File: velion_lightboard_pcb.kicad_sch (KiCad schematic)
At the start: 49 parts, among them J1 Conn_01x04, J10 Conn_01x03, J11 Conn_01x03, J2 Conn_01x04, J3 Conn_01x03, J4 Conn_01x03, J5 Conn_01x03, J6 Conn_01x03, J7 Conn_01x03, J8 Conn_01x03, J9 Conn_01x03, Q1 NMOS, Q2 NMOS, Q3 NMOS, Q4 NMOS, Q5 NMOS, Q6 NMOS, Q7 NMOS, Q8 NMOS, U1 TJA1051T-3, U6 ESP32-DEVKITC-32D, U7 MCP23017_SO, U8 MCP23017_SO

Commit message: switched MCU, implemented led driver, TODO : rangerfinder
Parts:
- removed R3, R4, R5: 100R, Resistor_SMD:R_1206_3216Metric_Pad1.30x1.75mm_HandSolder, symbol Device:R
- removed U6: ESP32-DEVKITC-32D, velion_mainboard:MODULE_ESP32-DEVKITC-32D, symbol ESP32-DEVKITC-32D:ESP32-DEVKITC-32D
- removed U7: MCP23017_SO, Package_SO:SOIC-28W_7.5x17.9mm_P1.27mm, symbol Interface_Expansion:MCP23017_SO
- added C3, C4: 100nF, symbol Device:C
- added J12: Conn_01x04, symbol Connector_Generic:Conn_01x04
- added LS1, LS2, LS3, LS4: Speaker_Ultrasound, symbol Device:Speaker_Ultrasound
- added U2, U3: ADS1115IDGS, Package_SO:TSSOP-10_3x3mm_P0.5mm, symbol Analog_ADC:ADS1115IDGS
- added U4: ESP32-C3_SUPERMINI_TH, ESP32-C3_SUPERMINI_TH:MODULE_ESP32-C3_SUPERMINI_TH, symbol ESP32-C3_SUPERMINI_TH:ESP32-C3_SUPERMINI_TH
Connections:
- net +3.3V: now also C3.1, C4.1, J12.3 (Pin_3), U2.8 (VDD), U3.1 (ADDR), U3.8 (VDD), U4.3.3 (3V3)
- net CAN_RX: now also U4.3 (GPIO3)
- net CAN_S: now also U4.7 (GPIO7)
- net CAN_TX: now also U4.2 (GPIO2)
- net GND: now also C3.2, C4.2, J12.4 (Pin_4), U2.1 (ADDR), U2.3 (GND), U3.3 (GND), U4.G (GND)
- net RGBLED_DIN: now also U4.8 (GPIO8)
- net SCL: now also J12.2 (Pin_2), U2.10 (SCL), U3.10 (SCL), U4.1 (GPIO1)
- net SDA: now also J12.1 (Pin_1), U2.9 (SDA), U3.9 (SDA), U4.0 (GPIO0)
- net MOSFET_GATE_0: now reaches U8.1 (GPB0)
- net MOSFET_GATE_0: now also Q6.1 (G)
- net MOSFET_GATE_1: now reaches U8.2 (GPB1)
- net MOSFET_GATE_1: now also Q5.1 (G)
- net MOSFET_GATE_2: now reaches U8.3 (GPB2)
- net MOSFET_GATE_2: now also Q4.1 (G)
- net MOSFET_GATE_3: now reaches U8.4 (GPB3)
- net MOSFET_GATE_3: now also Q3.1 (G)
- net MOSFET_GATE_4: now reaches U8.5 (GPB4)
- net MOSFET_GATE_4: now also Q2.1 (G)
- net MOSFET_GATE_5: now reaches U8.6 (GPB5)
- net MOSFET_GATE_5: now also Q1.1 (G)
- net MOSFET_GATE_6: now reaches U8.7 (GPB6)
- net MOSFET_GATE_6: now also Q8.1 (G)
- net MOSFET_GATE_7: now reaches U8.8 (GPB7)
- net MOSFET_GATE_7: now also Q7.1 (G)
- removed net LATCH_TRUNK_MOSFET_GATE: Q1.1 (G), Q2.1 (G), Q3.1 (G), Q4.1 (G), Q5.1 (G), Q6.1 (G), Q7.1 (G), Q8.1 (G)
- removed net SENSE: J10.3 (Pin_3), J11.3 (Pin_3), J4.3 (Pin_3), J5.3 (Pin_3), J6.3 (Pin_3), J7.3 (Pin_3), J8.3 (Pin_3), J9.3 (Pin_3), Q1.2 (S), Q2.2 (S), Q3.2 (S), Q4.2 (S), Q5.2 (S), Q6.2 (S), Q7.2 (S), Q8.2 (S), R14.1, R15.1, R16.1, R17.1, R19.1, R20.1, R21.1, R22.1
- new net SENSE_0: J10.3 (Pin_3), Q6.2 (S), R14.1, U2.4 (AIN0)
- new net SENSE_1: J9.3 (Pin_3), Q5.2 (S), R15.1, U2.5 (AIN1)
- new net SENSE_2: J8.3 (Pin_3), Q4.2 (S), R16.1, U2.6 (AIN2)
- new net SENSE_3: J7.3 (Pin_3), Q3.2 (S), R17.1, U2.7 (AIN3)
- new net SENSE_4: J6.3 (Pin_3), Q2.2 (S), R19.1, U3.4 (AIN0)
- new net SENSE_5: J5.3 (Pin_3), Q1.2 (S), R20.1, U3.5 (AIN1)
- new net SENSE_6: J4.3 (Pin_3), Q8.2 (S), R21.1, U3.6 (AIN2)
- new net SENSE_7: J11.3 (Pin_3), Q7.2 (S), R22.1, U3.7 (AIN3)
- no-connect marks 13 -> 5
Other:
- note added: "I2C addr : 1001000-> 0x48"
- note added: "I2C addr : 1001001-> 0x49"
- note added: "SDA SCL GND 3V3"
- note removed: "0100001 = 0x21"
- note removed: "leave serial port for debug"
- note removed: "resistor to limit risk of issue due to current leakage and the mosfet grid capacitor that could influence the strapping pin at boot."
- moved on the sheet: R6, R7

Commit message: Implemented piezo sonar driver
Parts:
- removed LS4: Speaker_Ultrasound, symbol Device:Speaker_Ultrasound
- added C10, C11, C12, C13, C14, C15, C16, C5, C6, C7, C8, C9: 100nF, symbol Device:C
- added D1, D2, D3, D6, D7, D8: D, symbol Device:D
- added J13, J14, J15: Conn_01x04, symbol Connector_Generic:Conn_01x04
- added Q10, Q11, Q12, Q13, Q14, Q15, Q16, Q17, Q18, Q19, Q20, Q9: BSS123-7-F, symbol Device:Q_NMOS
- added R23, R24, R25, R26, R27, R28, R29, R3, R30, R31, R4, R5: 470R, symbol Device:R
- added U10, U11, U5, U6, U7, U9: ~, symbol velion_mainboard:LM2104
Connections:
- net +12V: now also C12.1, C13.1, C16.1, C6.1, C7.1, C9.1, D1.2 (A), D2.2 (A), D3.2 (A), D6.2 (A), D7.2 (A), D8.2 (A), U10.1 (GVDD), U11.1 (GVDD), U5.1 (GVDD), U6.1 (GVDD), U7.1 (GVDD), U9.1 (GVDD)
- net +5V: now also U4.5V, J13.1 (Pin_1), J14.1 (Pin_1), J15.1 (Pin_1)
- net GND: now also C12.2, C13.2, C16.2, C6.2, C7.2, C9.2, J13.4 (Pin_4), J14.4 (Pin_4), J15.4 (Pin_4), Q10.S, Q12.S, Q14.S, Q16.S, Q18.S, Q20.S, U10.4 (GND), U11.4 (GND), U5.4 (GND), U6.4 (GND), U7.4 (GND), U9.4 (GND)
- net VBUS: now also Q11.D, Q13.D, Q15.D, Q17.D, Q19.D, Q9.D
- net ECHO_B: now reaches U4.10 (GPIO10)
- net ECHO_B: now also J14.3 (Pin_3)
- net ECHO_A: now reaches U4.20 (GPIO20)
- net ECHO_A: now also J15.3 (Pin_3)
- net TRIG_A: now reaches U4.4 (GPIO4)
- net TRIG_A: now also J15.2 (Pin_2)
- net TRIG_B: now reaches U4.5 (GPIO5)
- net TRIG_B: now also J14.2 (Pin_2)
- net TRIG_C: now reaches U4.6 (GPIO6)
- net TRIG_C: now also J13.2 (Pin_2)
- net ECHO_C: now reaches U4.9 (GPIO9)
- net ECHO_C: now also J13.3 (Pin_3)
- net EN_PIEZO_A: now reaches U8.21 (GPA0)
- net EN_PIEZO_A: now also U5.3 (~{SD}), U6.3 (~{SD})
- net EN_PIEZO_B: now reaches U8.22 (GPA1)
- net EN_PIEZO_B: now also U7.3 (~{SD}), U9.3 (~{SD})
- net EN_PIEZO_C: now reaches U8.23 (GPA2)
- net EN_PIEZO_C: now also U10.3 (~{SD}), U11.3 (~{SD})
- net EN_PIEZO_D: now reaches U8.24 (GPA3)
- net at LS1.1: now also Q13.S, Q14.D
- net at LS1.2: now also Q15.S, Q16.D
- net at LS3.1: now also Q10.D, Q9.S
- net at LS3.2: now also Q11.S, Q12.D
- net at LS2.1: now also Q17.S, Q18.D
- net at LS2.2: now also Q19.S, Q20.D
- new net: Q9.G, R3.2
- new net: R30.1, U11.5 (GL)
- new net: C15.2, U11.6 (SH)
- new net: R31.1, U11.7 (GH)
- new net: C15.1, D8.1 (K), U11.8 (BST)
- new net: Q16.G, R26.2
- new net: Q13.G, R24.2
- new net: Q19.G, R31.2
- new net: R23.1, U6.5 (GL)
- new net: Q12.G, R23.2
- new net: R25.1, U7.5 (GL)
- new net: C10.2, U7.6 (SH)
- new net: R24.1, U7.7 (GH)
- new net: C10.1, D3.1 (K), U7.8 (BST)
- new net: R29.1, U10.5 (GL)
- new net: C14.2, U10.6 (SH)
- new net: R28.1, U10.7 (GH)
- new net: C14.1, D7.1 (K), U10.8 (BST)
- new net: R5.1, U6.7 (GH)
- new net: Q11.G, R5.2
- new net: R3.1, U5.7 (GH)
- new net: C5.1, D1.1 (K), U5.8 (BST)
- new net: C5.2, U5.6 (SH)
- new net: R26.1, U9.5 (GL)
- new net: C11.2, U9.6 (SH)
- new net: R27.1, U9.7 (GH)
- new net: C11.1, D6.1 (K), U9.8 (BST)
- new net: Q10.G, R4.2
- new net: Q20.G, R30.2
- new net: Q18.G, R29.2
- new net: Q17.G, R28.2
- new net: C8.1, D2.1 (K), U6.8 (BST)
- new net: Q15.G, R27.2
- new net: C8.2, U6.6 (SH)
- new net: R4.1, U5.5 (GL)
- new net: Q14.G, R25.2
- new net PIEZO_PWM_HALF_X: U10.2 (IN), U5.2 (IN), U7.2 (IN)
- new net PIEZO_PWM_HALF_Y: U11.2 (IN), U6.2 (IN), U9.2 (IN)
- no-connect marks 5 -> 4
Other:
- note added: "3v3 come from ESP32-C internal regulator"
- note added: "5V TRIG ECHO GND"
- note added: "ADC for current sensing"
- note added: "GPIO"
- note added: "backup: if the driver dont work, we can use off the shelf module."
- note added: "classic bootstap capacitor setup"
- note added: "lightning"
- note added: "theses resistor are to limit EMI"
- note removed: "add ADC here with 8 channel"
- moved on the sheet: C3, C4, J12, U2, U3, U8

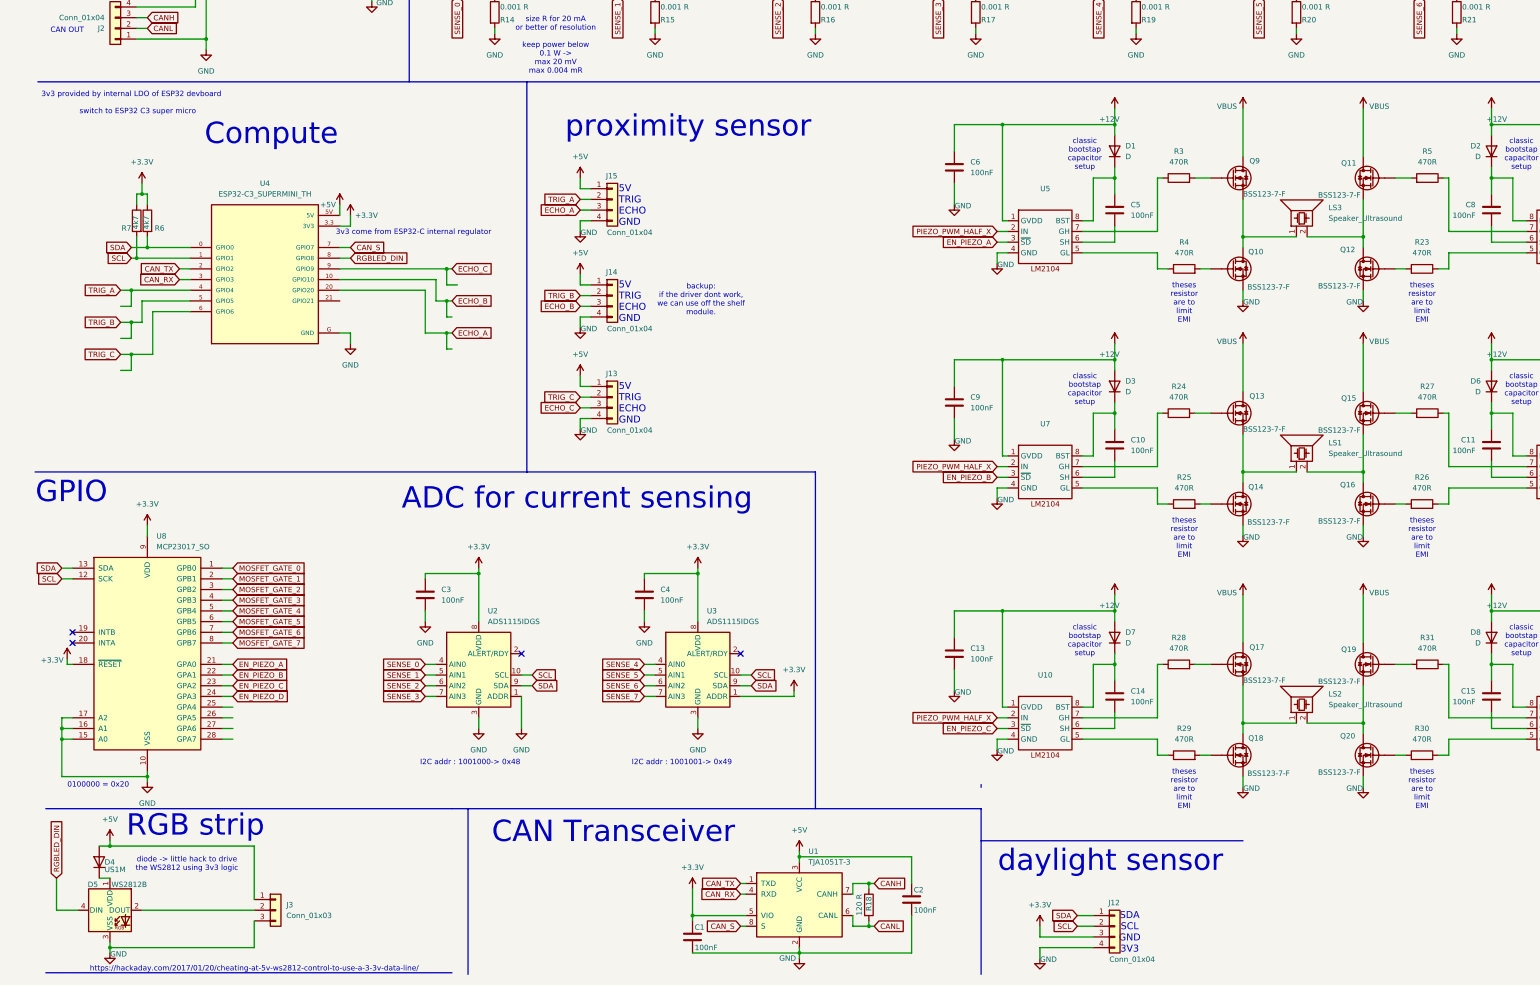
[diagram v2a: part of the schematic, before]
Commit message: implemented Analog stage for piezzo sonar
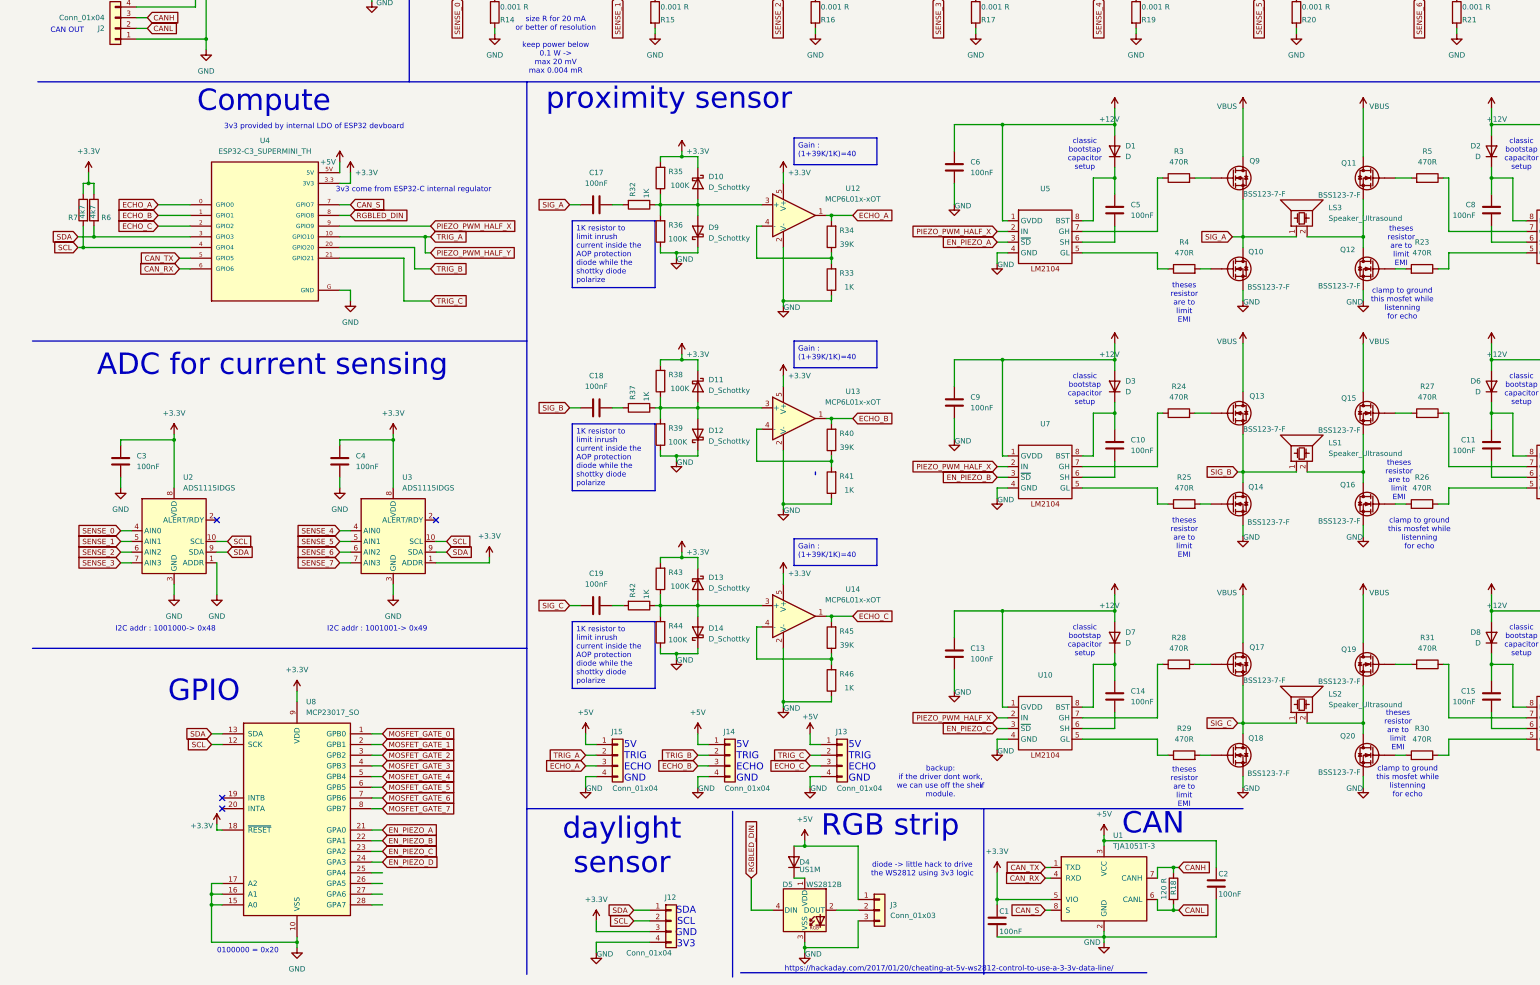
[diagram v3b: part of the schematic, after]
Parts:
- added C17, C18, C19: 100nF, symbol Device:C
- added D10, D11, D12, D13, D14, D9: D_Schottky, symbol Device:D_Schottky
- added R32, R33, R37, R41, R42, R46: 1K, symbol Device:R
- added R34, R40, R45: 39K, symbol Device:R
- added R35, R36, R38, R39, R43, R44: 100K, symbol Device:R
- added U12, U13, U14: MCP6L01x-xOT, Package_TO_SOT_SMD:SOT-23-5, symbol Amplifier_Operational:MCP6L01x-xOT
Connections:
- net +3.3V: now also D10.1 (K), D11.1 (K), D13.1 (K), R35.2, R38.2, R43.2, U12.5 (V+), U13.5 (V+), U14.5 (V+)
- net CAN_RX: now also U4.6 (GPIO6); no longer U4.3 (GPIO3)
- net CAN_TX: now also U4.5 (GPIO5); no longer U4.2 (GPIO2)
- net ECHO_A: now also U4.0 (GPIO0), R34.2, U12.1; no longer U4.20 (GPIO20)
- net ECHO_B: now also U4.1 (GPIO1), R40.2, U13.1; no longer U4.10 (GPIO10)
- net ECHO_C: now also U4.2 (GPIO2), R45.2, U14.1; no longer U4.9 (GPIO9)
- net GND: now also D12.1 (K), D14.1 (K), D9.1 (K), R33.1, R36.1, R39.1, R41.1, R44.1, R46.1, U12.2 (V-), U13.2 (V-), U14.2 (V-)
- net PIEZO_PWM_HALF_X: now also U4.9 (GPIO9)
- net PIEZO_PWM_HALF_Y: now also J15.2 (Pin_2), U4.10 (GPIO10)
- net SCL: now also U4.4 (GPIO4); no longer U4.1 (GPIO1)
- net SDA: now also U4.3 (GPIO3); no longer U4.0 (GPIO0)
- net TRIG_B: now also U4.20 (GPIO20); no longer U4.5 (GPIO5)
- net TRIG_C: now also U4.21 (GPIO21); no longer U4.6 (GPIO6)
- net SIG_A: now reaches LS3.1, Q10.D, Q9.S
- net SIG_A: now also C17.2
- net SIG_B: now reaches LS1.1, Q13.S, Q14.D
- net SIG_B: now also C18.2
- net SIG_C: now reaches LS2.1, Q17.S, Q18.D
- net SIG_C: now also C19.2
- removed net TRIG_A: J15.2 (Pin_2), U4.4 (GPIO4)
- new net: D13.2 (A), D14.2 (A), R42.1, R43.1, R44.2, U14.3 (+)
- new net: D11.2 (A), D12.2 (A), R37.1, R38.1, R39.2, U13.3 (+)
- new net: R45.1, R46.2, U14.4 (-)
- new net: R40.1, R41.2, U13.4 (-)
- new net: C18.1, R37.2
- new net: C17.1, R32.2
- new net: D10.2 (A), D9.2 (A), R32.1, R35.1, R36.2, U12.3 (+)
- new net: R33.2, R34.1, U12.4 (-)
- new net: C19.1, R42.2
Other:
- note added: "CAN"
- note added: "clamp to ground this mosfet while listenning for echo"
- note removed: "CAN Transceiver"
- note removed: "switch to ESP32 C3 super micro"
- moved on the sheet: C1, C2, C3, C4, D4, D5, J12, J13, J14, J15, J3, R18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

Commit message: layaing out the components
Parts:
- added J5, J6: Conn_01x04, velion_mainboard:15EDG-4P, symbol Connector_Generic:Conn_01x04
- C1: renamed from C9; footprint (none) -> Capacitor_SMD:C_1206_3216Metric_Pad1.33x1.80mm_HandSolder
- C10: renamed from C6; footprint (none) -> Capacitor_SMD:C_1206_3216Metric_Pad1.33x1.80mm_HandSolder
- C11: renamed from C5; footprint (none) -> Capacitor_SMD:C_1206_3216Metric_Pad1.33x1.80mm_HandSolder
- C12: renamed from C4; footprint (none) -> Capacitor_SMD:C_1206_3216Metric_Pad1.33x1.80mm_HandSolder
- C13: renamed from C14; footprint (none) -> Capacitor_SMD:C_1206_3216Metric_Pad1.33x1.80mm_HandSolder
- C14: renamed from C7; footprint (none) -> Capacitor_SMD:C_1206_3216Metric_Pad1.33x1.80mm_HandSolder
- C15: renamed from C17; footprint (none) -> Capacitor_SMD:C_1206_3216Metric_Pad1.33x1.80mm_HandSolder
- C16, C18, C19: footprint (none) -> Capacitor_SMD:C_1206_3216Metric_Pad1.33x1.80mm_HandSolder
- C17: renamed from C15; footprint (none) -> Capacitor_SMD:C_1206_3216Metric_Pad1.33x1.80mm_HandSolder
- C3: renamed from C10; footprint (none) -> Capacitor_SMD:C_1206_3216Metric_Pad1.33x1.80mm_HandSolder
- C4: renamed from C8; footprint (none) -> Capacitor_SMD:C_1206_3216Metric_Pad1.33x1.80mm_HandSolder
- C5: renamed from C3; footprint (none) -> Capacitor_SMD:C_1206_3216Metric_Pad1.33x1.80mm_HandSolder
- C7: renamed from C13; footprint (none) -> Capacitor_SMD:C_1206_3216Metric_Pad1.33x1.80mm_HandSolder
- C8: renamed from C12; footprint (none) -> Capacitor_SMD:C_1206_3216Metric_Pad1.33x1.80mm_HandSolder
- C9: renamed from C11; footprint (none) -> Capacitor_SMD:C_1206_3216Metric_Pad1.33x1.80mm_HandSolder
- D10: renamed from D3; footprint (none) -> Diode_SMD:D_SMA
- D11: renamed from D6; footprint (none) -> Diode_SMD:D_SMA
- D13: renamed from D8; footprint (none) -> Diode_SMD:D_SMA
- D14: renamed from D7; footprint (none) -> Diode_SMD:D_SMA
- D2: renamed from D9; value D_Schottky -> RB551V-30-HF; footprint (none) -> Diode_SMD:D_SOD-323_HandSoldering
- D3: renamed from D10; value D_Schottky -> RB551V-30-HF; footprint (none) -> Diode_SMD:D_SOD-323_HandSoldering
- D4: renamed from D11; value D_Schottky -> RB551V-30-HF; footprint (none) -> Diode_SMD:D_SOD-323_HandSoldering
- D5: renamed from D12; value D_Schottky -> RB551V-30-HF; footprint (none) -> Diode_SMD:D_SOD-323_HandSoldering
- D6: renamed from D13; value D_Schottky -> RB551V-30-HF; footprint (none) -> Diode_SMD:D_SOD-323_HandSoldering
- D7: renamed from D14; value D_Schottky -> RB551V-30-HF; footprint (none) -> Diode_SMD:D_SOD-323_HandSoldering
- D8: renamed from D2; footprint (none) -> Diode_SMD:D_SMA
- D9: renamed from D1; footprint (none) -> Diode_SMD:D_SMA
- J10: renamed from J14; footprint (none) -> Connector_PinHeader_2.54mm:PinHeader_1x04_P2.54mm_Vertical
- J11: renamed from J12; footprint (none) -> Connector_PinHeader_2.54mm:PinHeader_1x04_P2.54mm_Vertical
- J12: renamed from J6; footprint (none) -> velion_mainboard:15EDG-3P
- J13: renamed from J5; footprint (none) -> velion_mainboard:15EDG-3P
- J14: renamed from J3; footprint (none) -> velion_mainboard:15EDG-3P
- J15: renamed from J4; footprint (none) -> velion_mainboard:15EDG-3P
- J16: renamed from J11; footprint (none) -> velion_mainboard:15EDG-3P
- J17: renamed from J13; footprint (none) -> Connector_PinHeader_2.54mm:PinHeader_1x04_P2.54mm_Vertical
- J3: renamed from J10; footprint (none) -> velion_mainboard:15EDG-3P
- J4: renamed from J15; footprint (none) -> Connector_PinHeader_2.54mm:PinHeader_1x04_P2.54mm_Vertical
- J7: renamed from J9; footprint (none) -> velion_mainboard:15EDG-3P
- J8: footprint (none) -> velion_mainboard:15EDG-3P
- J9: renamed from J7; footprint (none) -> velion_mainboard:15EDG-3P
- LS1: renamed from LS3; footprint (none) -> velion_mainboard:15EDG-2P
- LS2: renamed from LS1; footprint (none) -> velion_mainboard:15EDG-2P
- LS3: renamed from LS2; footprint (none) -> velion_mainboard:15EDG-2P
- Q1: renamed from Q9; footprint (none) -> velion_mainboard:BSS123_TSOT-23_HandSoldering
- Q10: renamed from Q17; footprint (none) -> velion_mainboard:BSS123_TSOT-23_HandSoldering
- Q11: renamed from Q20; footprint (none) -> velion_mainboard:BSS123_TSOT-23_HandSoldering
- Q12: renamed from Q19; footprint (none) -> velion_mainboard:BSS123_TSOT-23_HandSoldering
- Q2: renamed from Q10; footprint (none) -> velion_mainboard:BSS123_TSOT-23_HandSoldering
- Q3: renamed from Q14; footprint (none) -> velion_mainboard:BSS123_TSOT-23_HandSoldering
- Q4: renamed from Q13; footprint (none) -> velion_mainboard:BSS123_TSOT-23_HandSoldering
- Q5: renamed from Q11; footprint (none) -> velion_mainboard:BSS123_TSOT-23_HandSoldering
- Q6: renamed from Q16; footprint (none) -> velion_mainboard:BSS123_TSOT-23_HandSoldering
- Q7: renamed from Q15; footprint (none) -> velion_mainboard:BSS123_TSOT-23_HandSoldering
- Q8: renamed from Q12; footprint (none) -> velion_mainboard:BSS123_TSOT-23_HandSoldering
- Q9: renamed from Q18; footprint (none) -> velion_mainboard:BSS123_TSOT-23_HandSoldering
- R1: renamed from R3; footprint (none) -> Resistor_SMD:R_1206_3216Metric_Pad1.30x1.75mm_HandSolder
- R10: renamed from R26; footprint (none) -> Resistor_SMD:R_1206_3216Metric_Pad1.30x1.75mm_HandSolder
- R11: renamed from R29; footprint (none) -> Resistor_SMD:R_1206_3216Metric_Pad1.30x1.75mm_HandSolder
- R12: renamed from R30; footprint (none) -> Resistor_SMD:R_1206_3216Metric_Pad1.30x1.75mm_HandSolder
- R13: renamed from R41; footprint (none) -> Resistor_SMD:R_1206_3216Metric_Pad1.30x1.75mm_HandSolder
- R14: renamed from R40; footprint (none) -> Resistor_SMD:R_1206_3216Metric_Pad1.30x1.75mm_HandSolder
- R15: renamed from R39; footprint (none) -> Resistor_SMD:R_1206_3216Metric_Pad1.30x1.75mm_HandSolder
- R16: renamed from R31; footprint (none) -> Resistor_SMD:R_1206_3216Metric_Pad1.30x1.75mm_HandSolder
- R17: renamed from R43; footprint (none) -> Resistor_SMD:R_1206_3216Metric_Pad1.30x1.75mm_HandSolder
- R18: renamed from R34; footprint (none) -> Resistor_SMD:R_1206_3216Metric_Pad1.30x1.75mm_HandSolder
- R19: renamed from R33; footprint (none) -> Resistor_SMD:R_1206_3216Metric_Pad1.30x1.75mm_HandSolder
- R20: renamed from R32; footprint (none) -> Resistor_SMD:R_1206_3216Metric_Pad1.30x1.75mm_HandSolder
- R21: renamed from R45; footprint (none) -> Resistor_SMD:R_1206_3216Metric_Pad1.30x1.75mm_HandSolder
- R22: renamed from R44; footprint (none) -> Resistor_SMD:R_1206_3216Metric_Pad1.30x1.75mm_HandSolder
- R23: renamed from R42; footprint (none) -> Resistor_SMD:R_1206_3216Metric_Pad1.30x1.75mm_HandSolder
- R24: renamed from R35; footprint (none) -> Resistor_SMD:R_1206_3216Metric_Pad1.30x1.75mm_HandSolder
- R25: renamed from R46; footprint (none) -> Resistor_SMD:R_1206_3216Metric_Pad1.30x1.75mm_HandSolder
- R26: renamed from R37; footprint (none) -> Resistor_SMD:R_1206_3216Metric_Pad1.30x1.75mm_HandSolder
- R27: renamed from R38; footprint (none) -> Resistor_SMD:R_1206_3216Metric_Pad1.30x1.75mm_HandSolder
- R28: renamed from R36; footprint (none) -> Resistor_SMD:R_1206_3216Metric_Pad1.30x1.75mm_HandSolder
- R29: renamed from R13; footprint (none) -> Resistor_SMD:R_1206_3216Metric_Pad1.30x1.75mm_HandSolder
- R3: renamed from R5; footprint (none) -> Resistor_SMD:R_1206_3216Metric_Pad1.30x1.75mm_HandSolder
- R30: renamed from R22; footprint (none) -> Resistor_SMD:R_2512_6332Metric_Pad1.40x3.35mm_HandSolder
- R31: renamed from R1; footprint (none) -> Resistor_SMD:R_1206_3216Metric_Pad1.30x1.75mm_HandSolder
- R34: renamed from R2; footprint (none) -> Resistor_SMD:R_1206_3216Metric_Pad1.30x1.75mm_HandSolder
- R35: renamed from R21; footprint (none) -> Resistor_SMD:R_2512_6332Metric_Pad1.40x3.35mm_HandSolder
- R36: renamed from R20; footprint (none) -> Resistor_SMD:R_2512_6332Metric_Pad1.40x3.35mm_HandSolder
- R37: renamed from R8; footprint (none) -> Resistor_SMD:R_1206_3216Metric_Pad1.30x1.75mm_HandSolder
- R38: renamed from R19; footprint (none) -> Resistor_SMD:R_2512_6332Metric_Pad1.40x3.35mm_HandSolder
- R39: renamed from R9; footprint (none) -> Resistor_SMD:R_1206_3216Metric_Pad1.30x1.75mm_HandSolder
- R4: footprint (none) -> Resistor_SMD:R_1206_3216Metric_Pad1.30x1.75mm_HandSolder
- R40: renamed from R17; footprint (none) -> Resistor_SMD:R_2512_6332Metric_Pad1.40x3.35mm_HandSolder
- R41: renamed from R10; footprint (none) -> Resistor_SMD:R_1206_3216Metric_Pad1.30x1.75mm_HandSolder
- R42: renamed from R16; footprint (none) -> Resistor_SMD:R_2512_6332Metric_Pad1.40x3.35mm_HandSolder
- R43: renamed from R11; footprint (none) -> Resistor_SMD:R_1206_3216Metric_Pad1.30x1.75mm_HandSolder
- R44: renamed from R15; footprint (none) -> Resistor_SMD:R_2512_6332Metric_Pad1.40x3.35mm_HandSolder
- R45: renamed from R12; footprint (none) -> Resistor_SMD:R_1206_3216Metric_Pad1.30x1.75mm_HandSolder
- R46: renamed from R14; footprint (none) -> Resistor_SMD:R_2512_6332Metric_Pad1.40x3.35mm_HandSolder
- R5: renamed from R25; footprint (none) -> Resistor_SMD:R_1206_3216Metric_Pad1.30x1.75mm_HandSolder
- R6: renamed from R24; footprint (none) -> Resistor_SMD:R_1206_3216Metric_Pad1.30x1.75mm_HandSolder
- R7: renamed from R23; footprint (none) -> Resistor_SMD:R_1206_3216Metric_Pad1.30x1.75mm_HandSolder
- R8: renamed from R28; footprint (none) -> Resistor_SMD:R_1206_3216Metric_Pad1.30x1.75mm_HandSolder
- R9: renamed from R27; footprint (none) -> Resistor_SMD:R_1206_3216Metric_Pad1.30x1.75mm_HandSolder
- U1: renamed from U4; footprint ESP32-C3_SUPERMINI_TH:MODULE_ESP32-C3_SUPERMINI_TH -> velion_mainboard:MODULE_ESP32-C3_SUPERMINI_TH
- U10: renamed from U11; value ~ -> LM2104DR; footprint (none) -> Package_SO:SO-8_3.9x4.9mm_P1.27mm
- U5, U6, U7: value ~ -> LM2104DR; footprint (none) -> Package_SO:SO-8_3.9x4.9mm_P1.27mm
- U8: renamed from U9; value ~ -> LM2104DR; footprint (none) -> Package_SO:SO-8_3.9x4.9mm_P1.27mm
- U9: renamed from U10; value ~ -> LM2104DR; footprint (none) -> Package_SO:SO-8_3.9x4.9mm_P1.27mm
- renumbered C1 to C2, C2 to C6, D5 to D1, D4 to D12, Q7 to Q13, Q8 to Q14, Q1 to Q15, Q2 to Q16, Q3 to Q17, Q4 to Q18, Q5 to Q19, Q6 to Q20, R18 to R2, R7 to R32, R6 to R33, U3 to U11, U8 to U12, U2 to U13, U1 to U14, U13 to U2, U12 to U3, U14 to U4
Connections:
- net +12V: now also J6.4 (Pin_4)
- net +5V: now also J5.4 (Pin_4)
- net GND: now also J5.2 (Pin_2), J5.3 (Pin_3), J6.2 (Pin_2), J6.3 (Pin_3)
- net MOSFET_GATE_0: now also U12.8 (GPB7); no longer U12.1 (GPB0)
- net MOSFET_GATE_1: now also U12.7 (GPB6); no longer U12.2 (GPB1)
- net MOSFET_GATE_2: now also U12.6 (GPB5); no longer U12.3 (GPB2)
- net MOSFET_GATE_3: now also U12.5 (GPB4); no longer U12.4 (GPB3)
- net MOSFET_GATE_4: now also U12.4 (GPB3); no longer U12.5 (GPB4)
- net MOSFET_GATE_5: now also U12.3 (GPB2); no longer U12.6 (GPB5)
- net MOSFET_GATE_6: now also U12.2 (GPB1); no longer U12.7 (GPB6)
- net MOSFET_GATE_7: now also U12.1 (GPB0); no longer U12.8 (GPB7)
- net SENSE_0: now also U13.7 (AIN3); no longer U13.4 (AIN0)
- net SENSE_1: now also U13.6 (AIN2); no longer U13.5 (AIN1)
- net SENSE_2: now also U13.5 (AIN1); no longer U13.6 (AIN2)
- net SENSE_3: now also U13.4 (AIN0); no longer U13.7 (AIN3)
- net SENSE_4: now also U11.7 (AIN3); no longer U11.4 (AIN0)
- net SENSE_5: now also U11.6 (AIN2); no longer U11.5 (AIN1)
- net SENSE_6: now also U11.5 (AIN1); no longer U11.6 (AIN2)
- net SENSE_7: now also U11.4 (AIN0); no longer U11.7 (AIN3)
- net VBUS: now also J5.1 (Pin_1), J6.1 (Pin_1)
- net EN_PIEZO_D: no longer names the net of U12.24 (GPA3)
- no-connect marks 4 -> 9
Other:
- note added: "5A MAX -> 60W light"
- note added: "ADC pins"
- note added: "DC Buck 80 V to 12V 10 A"
- note added: "DC Buck 80 V to 5V 1 A (if we implement RGB strip, get 10A)"
- note added: "H bridge to double effective voltage , improve range. No transformer required since we have a main bus at 48V"
- note added: "HV mosfet (100V+) small current (100 mA)"
- note added: "classic bootstap capacitor setup (100V reverse polarity minimum)"
- note added: "https://de.aliexpress.com/item/1005005829877910.html"
- note added: "https://de.aliexpress.com/item/1005009210793105.html"
- note added: "theses resistor are to limit EMI. samge logic for the resistor in serie with OpAmp"
- note added: "this is mainly to detect fault in the lightning system (dead lamp) but it can also be used (crudelly) if one choose to do PWM to dim the light and control the current"
- note added: "trig used only if we choose off the shelf module instead"
- note removed: "theses resistor are to limit EMI"
- moved on the sheet: C14, C16, C17, C4, C8, C9, D11, D13, D8, Q11, Q12, Q5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

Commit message: routed the PCB, need review
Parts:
- renumbered C19 to C0, C7 to C1, C1 to C10, C9 to C11, C3 to C12, C8 to C13, C10 to C14, C4 to C15, C11 to C16, C14 to C17, C12 to C18, C16 to C2, C13 to C3, C17 to C4, C18 to C6, C6 to C7, C2 to C8, C15 to C9, D12 to D0, D3 to D10, D9 to D12, D8 to D13, D7 to D2, D6 to D3, D14 to D4, D13 to D5, D5 to D6, D4 to D7, D10 to D8, D2 to D9, J9 to J10, J10 to J11, J11 to J12, J15 to J13, J13 to J14, J14 to J15, J12 to J9, LS3 to LS1, LS1 to LS2, LS2 to LS3, Q13 to Q0, Q10 to Q1, Q7 to Q10, Q16 to Q11, Q17 to Q12, Q2 to Q13, Q1 to Q14, Q8 to Q15, Q5 to Q16, Q18 to Q17, Q19 to Q18, Q20 to Q19, Q9 to Q2, Q12 to Q3, Q11 to Q4, Q14 to Q5, Q15 to Q6, Q3 to Q7, Q4 to Q8, Q6 to Q9, R29 to R0, R30 to R1, R12 to R10, R22 to R11, R25 to R12, R36 to R13, R34 to R14, R35 to R15, R31 to R16, R26 to R17, R6 to R18, R9 to R19, R32 to R2, R10 to R20, R5 to R21, R14 to R22, R13 to R23, R27 to R24, R15 to R25, R38 to R26, R40 to R27, R39 to R28, R37 to R29, R33 to R3, R20 to R30, R19 to R31, R24 to R32, R18 to R33, R28 to R34, R43 to R35, R42 to R36, R41 to R37, R44 to R38, R2 to R39, R11 to R4, R4 to R40, R1 to R41, R7 to R42, R3 to R43, R45 to R44, R46 to R45, R23 to R5, R17 to R6, R8 to R7, R21 to R8, R16 to R9, U3 to U10, U8 to U11, U5 to U12, U6 to U13, U13 to U14, U12 to U2, U10 to U3, U9 to U4, U4 to U5, U11 to U6, U2 to U7, U14 to U8, U7 to U9
